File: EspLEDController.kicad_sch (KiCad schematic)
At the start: 22 parts, among them J1 USB_B_Micro, J2 FTDI, J3 FLASH, SW1 RESET, SW2 FLASH, U1 ESP-12F, U17 74AHCT1G125, U2 AMS1117-3.3

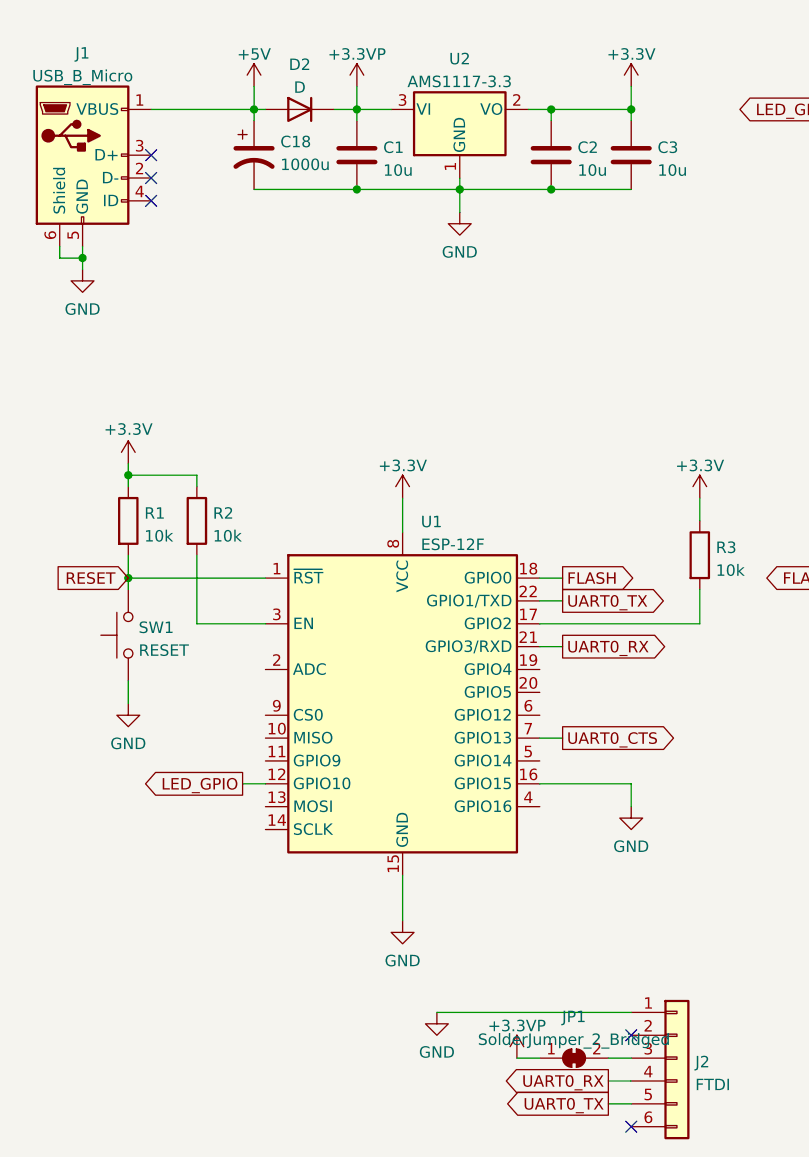
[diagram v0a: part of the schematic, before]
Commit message: v1.1 Fix LED headers, FTDI power
Fixes from first board rev:
	- Fix LEDs to be between power and driver output
	- Change FTDI header power to 5V
	- Remove now redundant diode on FTDI power input
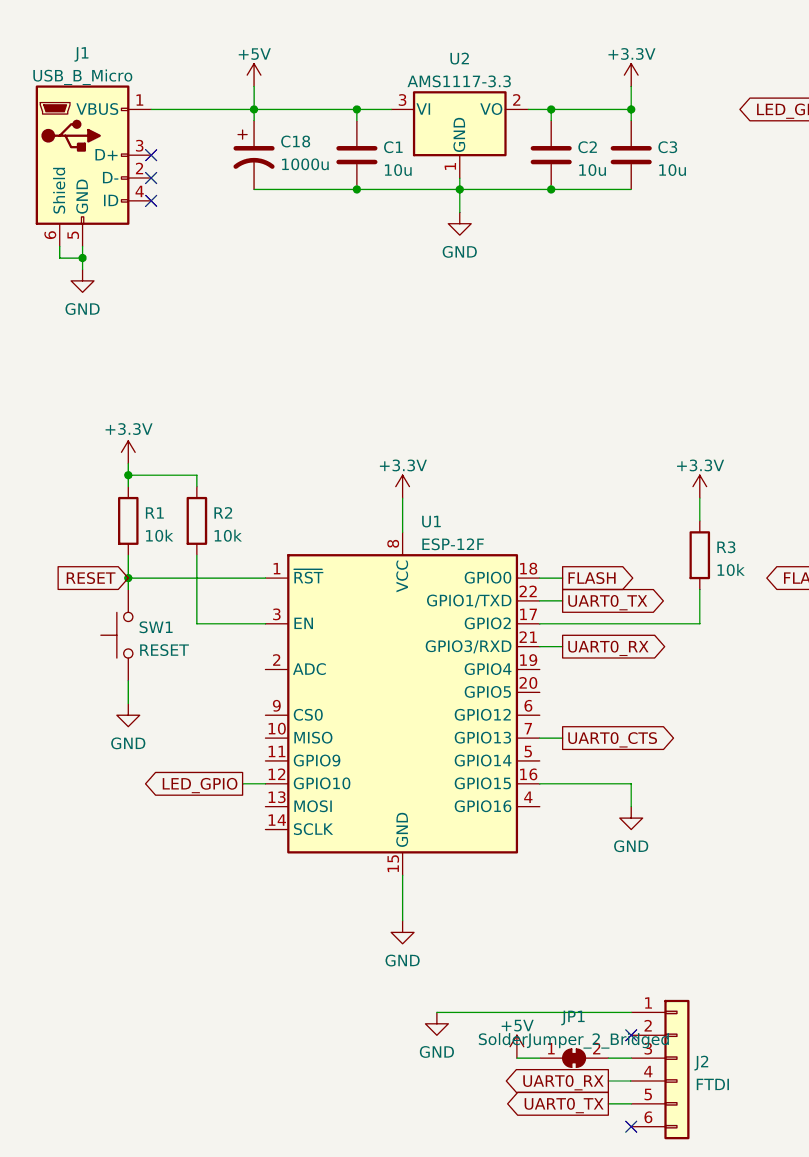
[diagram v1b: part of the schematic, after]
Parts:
- removed D2: D, Diode_SMD:D_SMA, symbol Device:D
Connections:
- net +3.3VP is gone; now on net +5V: C1.1, JP1.1 (A), U2.3 (VI)

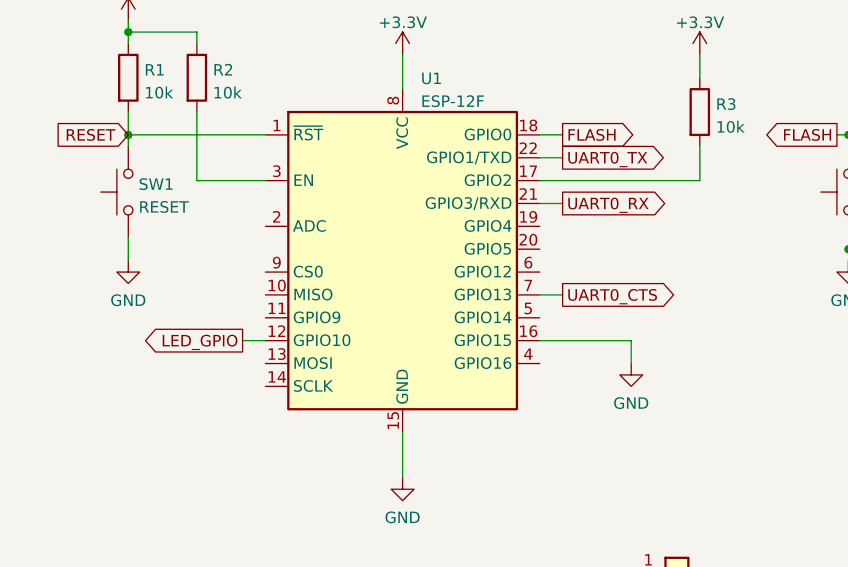
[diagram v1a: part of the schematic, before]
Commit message: Fix incorrect ESP8266 GPIO pin
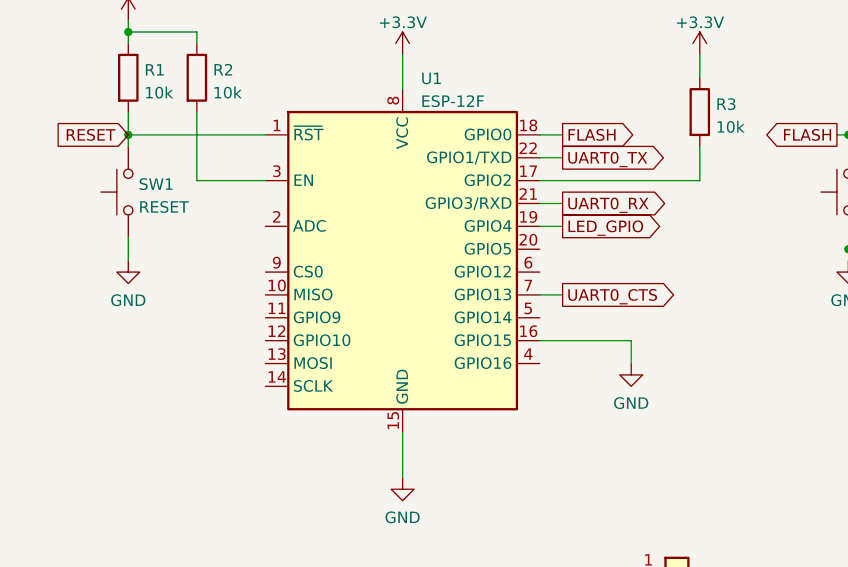
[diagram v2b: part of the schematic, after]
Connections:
- net LED_GPIO: now also U1.19 (GPIO4); no longer U1.12 (GPIO10)
